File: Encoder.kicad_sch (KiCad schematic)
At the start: 12 parts, among them J1 Conn_01x05_Pin, SW1 RotaryEncoder_Switch_MP, U1 74LVC3G14

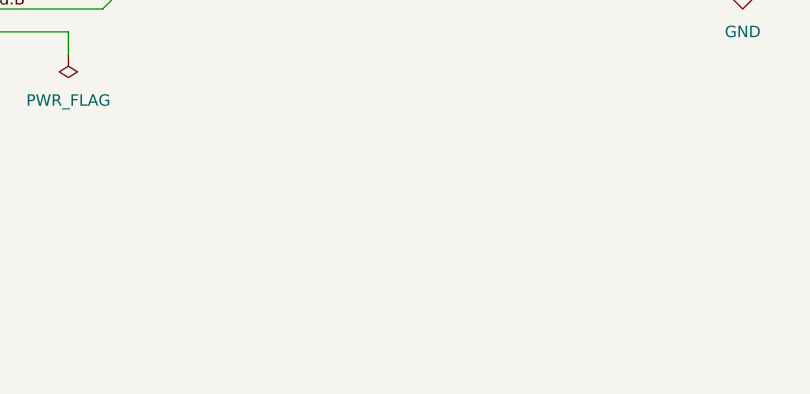
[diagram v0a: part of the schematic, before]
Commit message: Add mounting holes
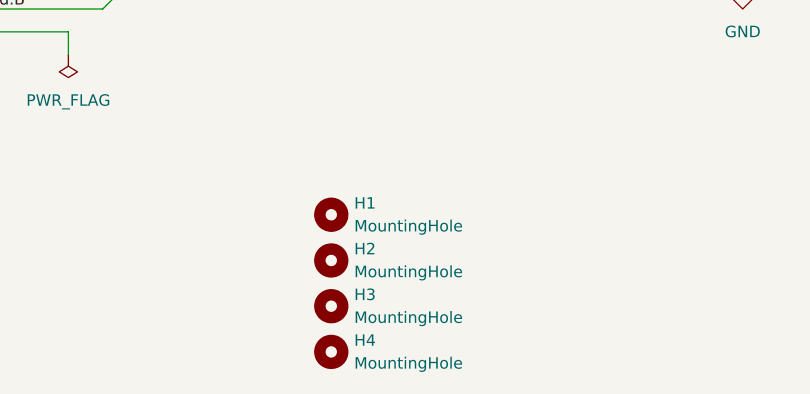
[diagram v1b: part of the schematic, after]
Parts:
- added H1, H2, H3, H4: MountingHole, MountingHole:MountingHole_2mm, symbol Mechanical:MountingHole

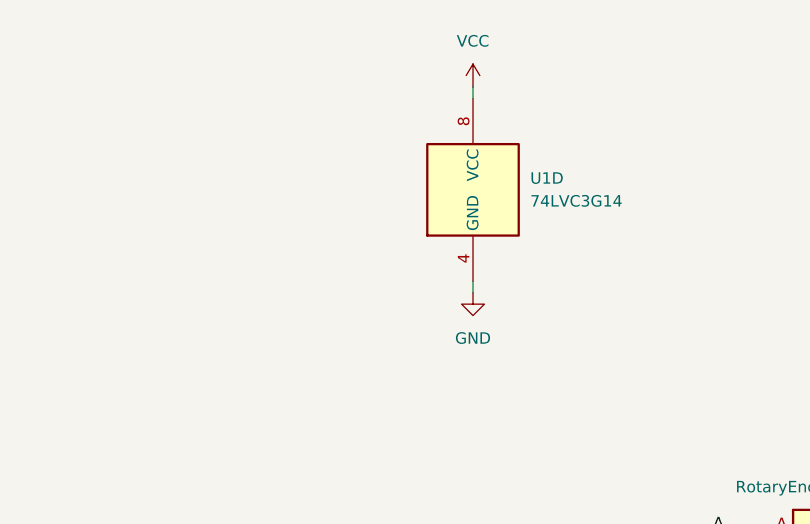
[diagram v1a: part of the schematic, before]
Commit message: Add decoupling capacitor
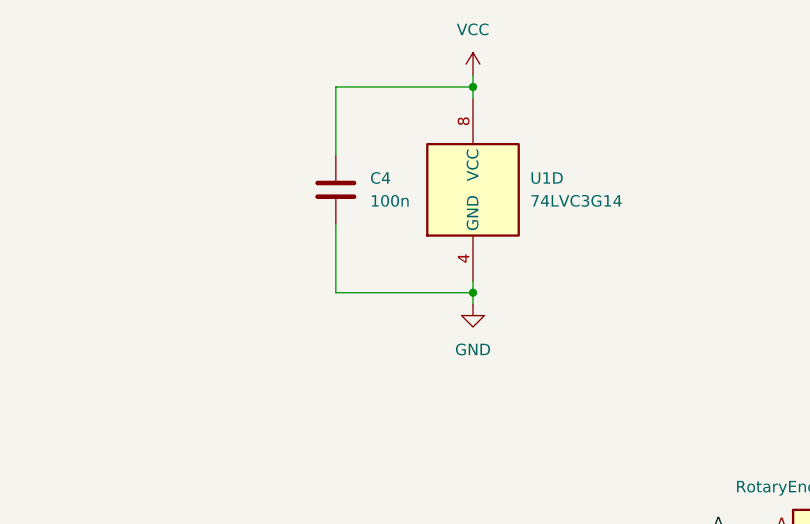
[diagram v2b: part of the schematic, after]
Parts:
- added C4: 100n, Capacitor_SMD:C_1206_3216Metric_Pad1.33x1.80mm_HandSolder, symbol Device:C
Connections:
- net GND: now also C4.2
- net VCC: now also C4.1

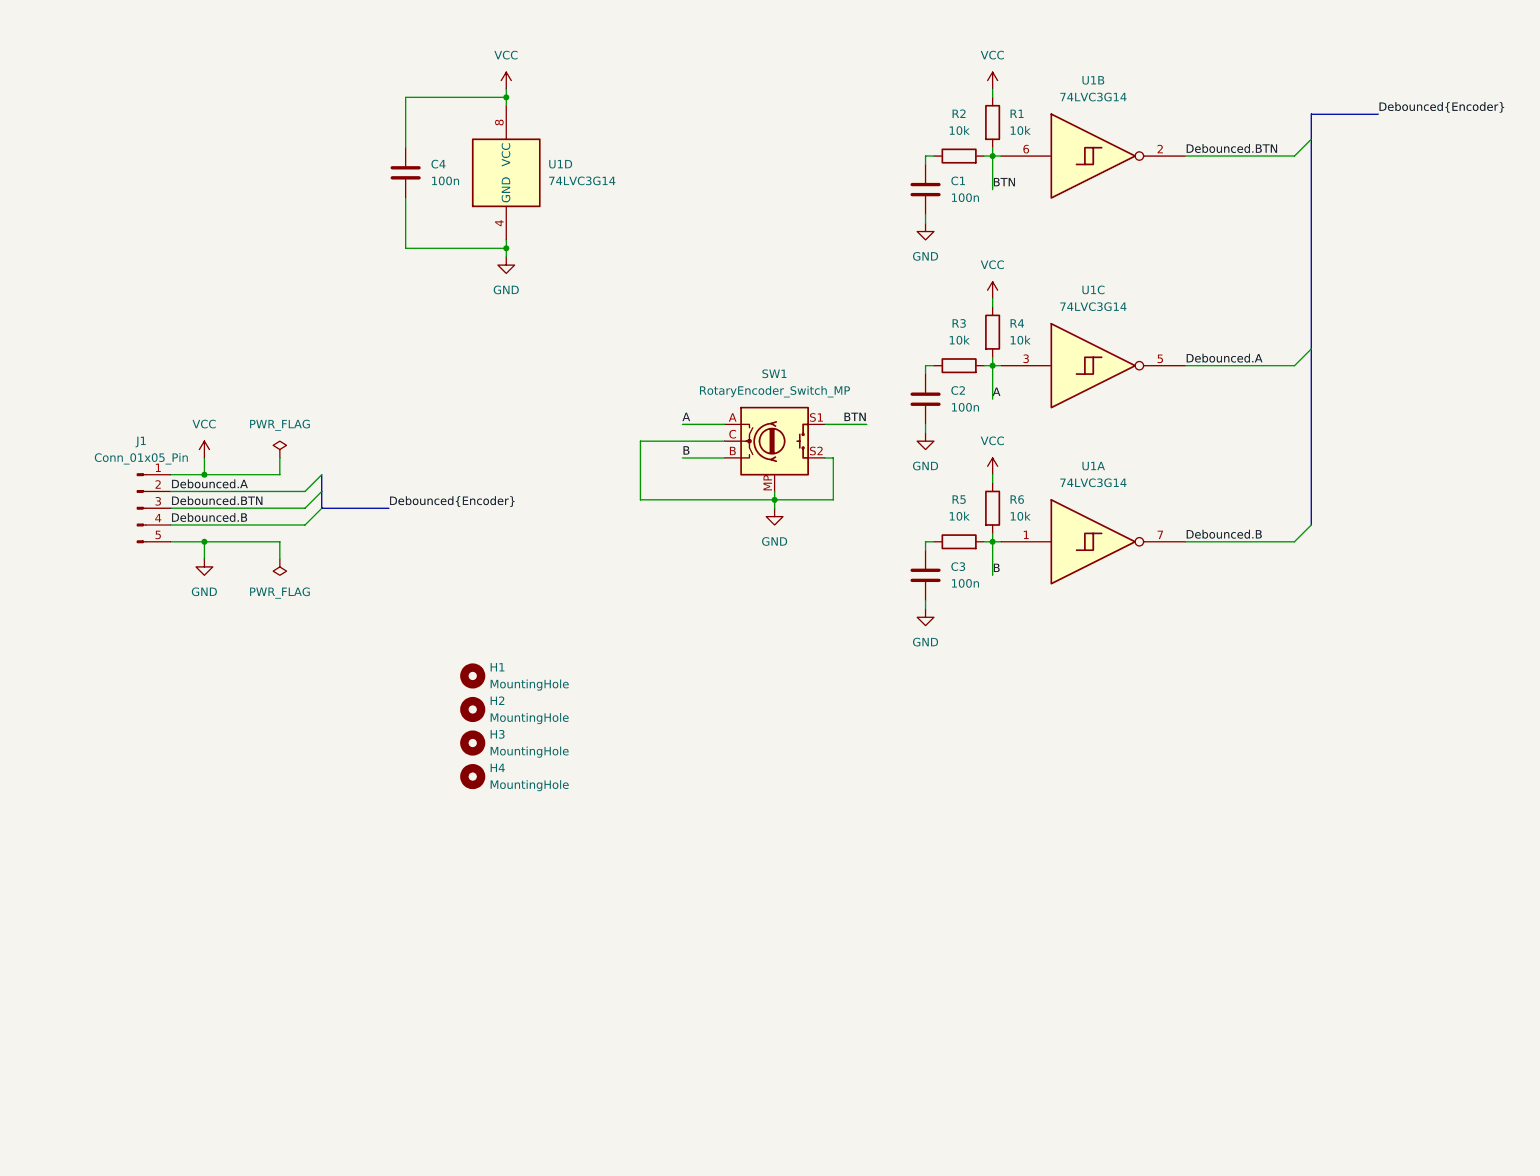
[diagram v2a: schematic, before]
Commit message: Fix debounce routing
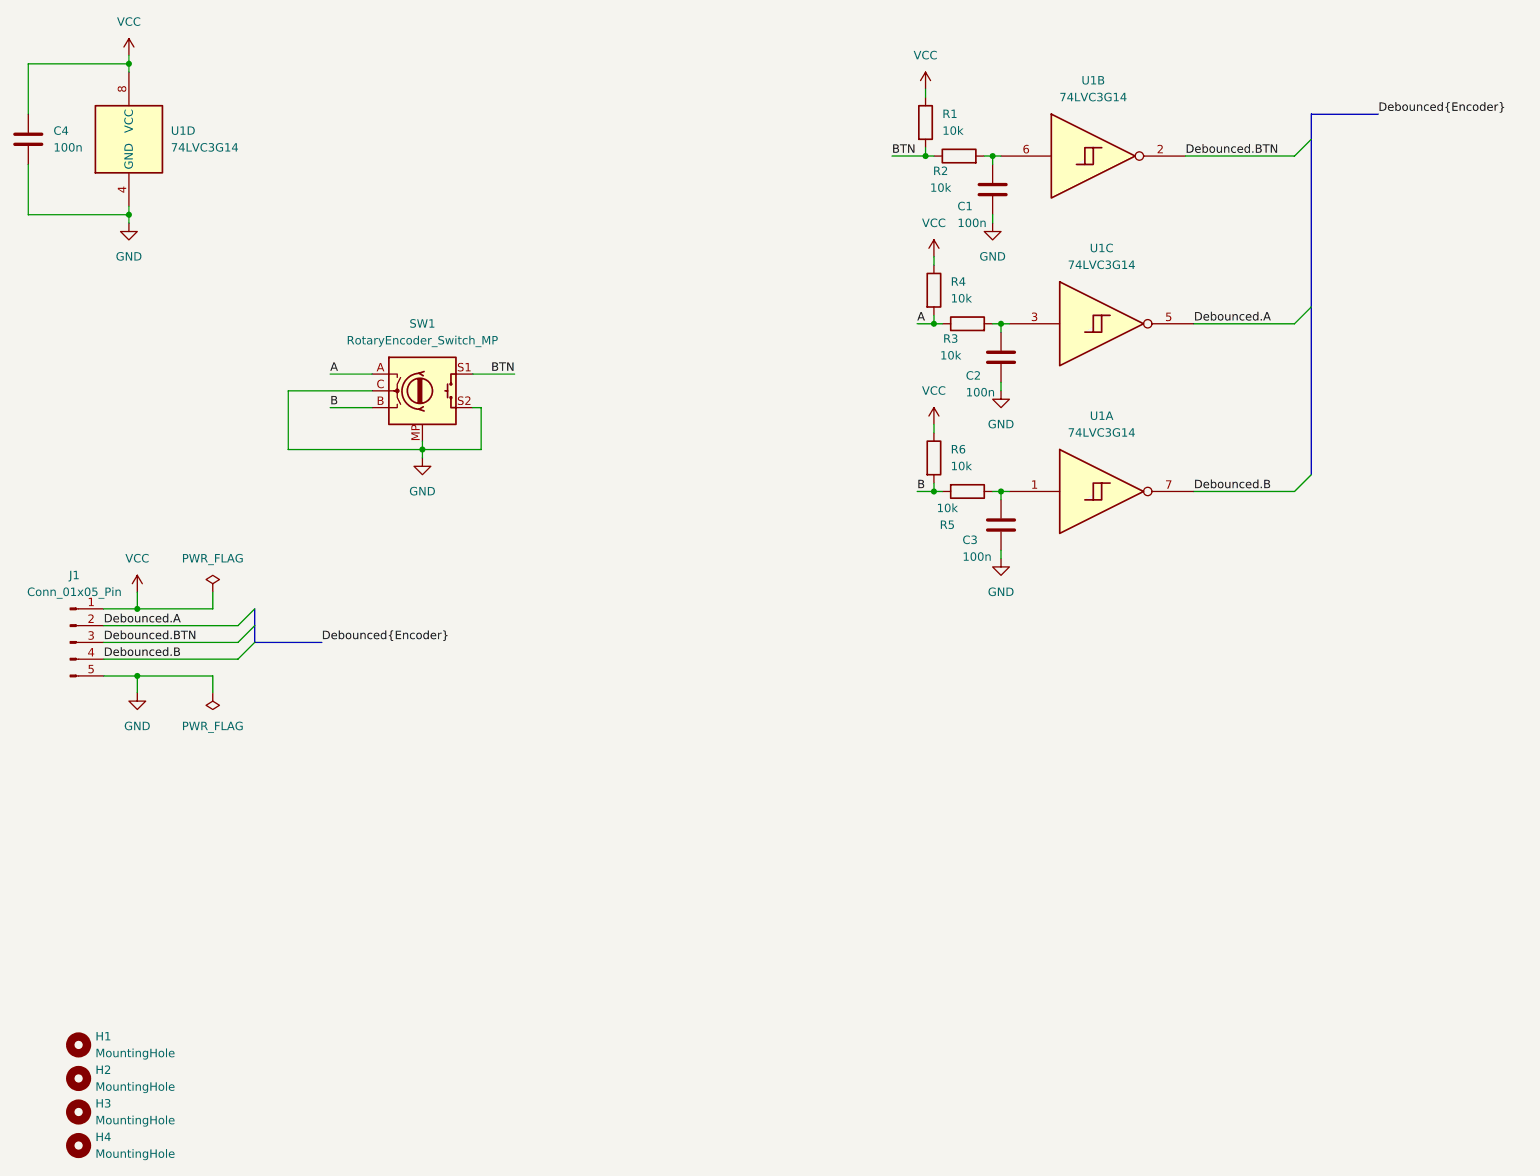
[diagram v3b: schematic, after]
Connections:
- net A: now also R3.1; no longer R3.2, U1.3
- net B: no longer U1.1
- net BTN: now also R2.1; no longer R2.2, U1.6
- net at C3.1, R5.1: now also U1.1
- net at C2.1: now also R3.2, U1.3; no longer R3.1
- net at C1.1: now also R2.2, U1.6; no longer R2.1
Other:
- moved on the sheet: C1, C2, C3, C4, H1, H2, H3, H4, J1, R1, R3, R4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
